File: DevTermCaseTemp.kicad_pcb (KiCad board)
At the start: 2 copper layers, 98.2 x 88.6 mm, 79 parts, among them J1 USB_A, J11 Conn_01x06, J2 EXT_miniPCIe, J3 USB_A, J4 USB_B_Micro, J5 Conn_01x02, J7 DevTermSpeaker, J8 DevTermSpeaker, J9 Conn_02x22_Odd_Even, M2 DevTerm Stock Fan, Q1 BSS138, SW1 SW_DIP_x02, SW2 SW_SPDT, U1 GL850G, U10 4052, U11 4052, U12 TXS0102DCT, U13 USBLC6-2P6, U14 USBLC6-2P6, U15 USBLC6-2P6, U16 USBLC6-2P6, U17 USBLC6-2P6, U18 USBLC6-2P6, U2 SY6280, U3 SY6280, U4 DS1307+, U5 MCP23008-xSO, U6 CH340N, U7 4052, U8 4052, U9 EMC2301-1-ACZL-TR, Y1 12MHz, Y2 32.768KHz

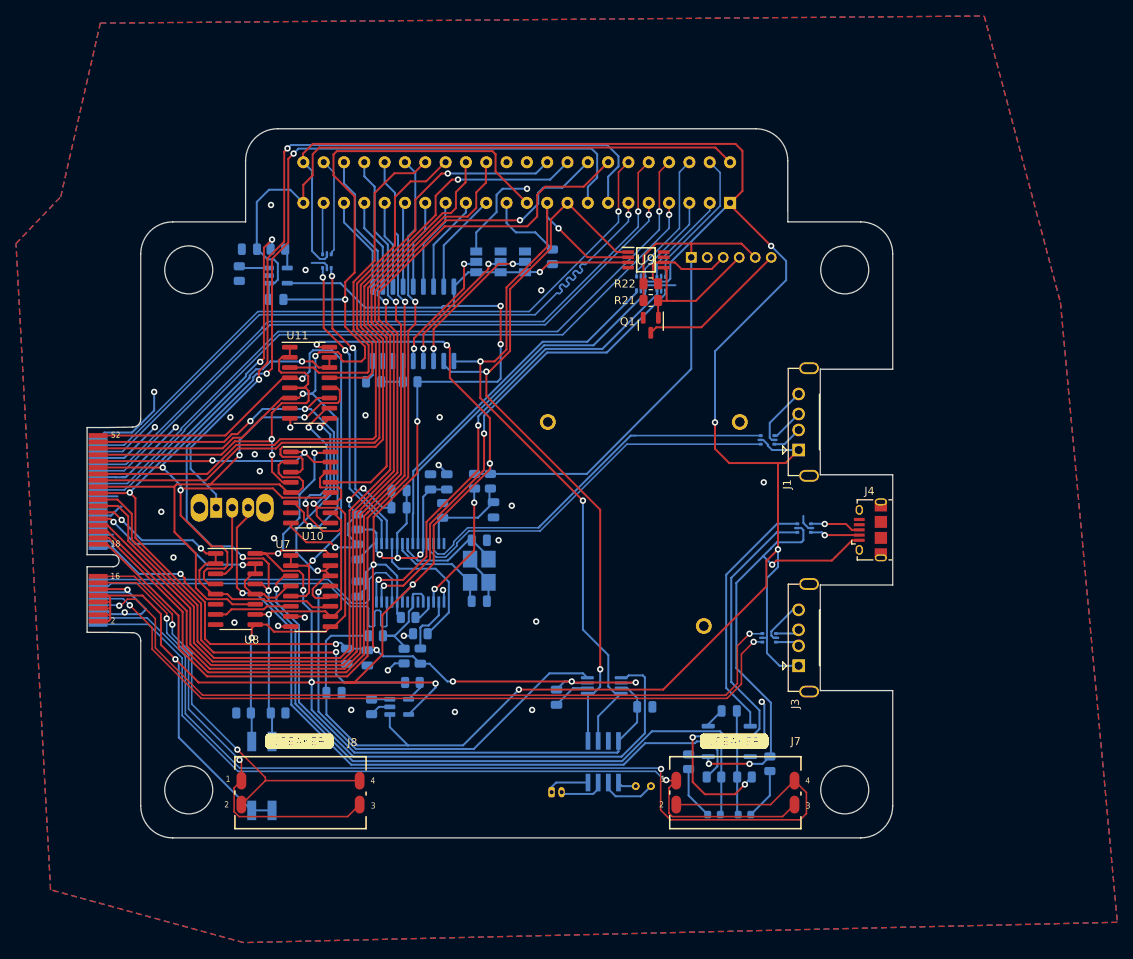
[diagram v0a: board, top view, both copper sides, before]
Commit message: Added bypass caps for USB ESD surge protection as specified in datasheet.
+ Updated silkscreen for version and serial number
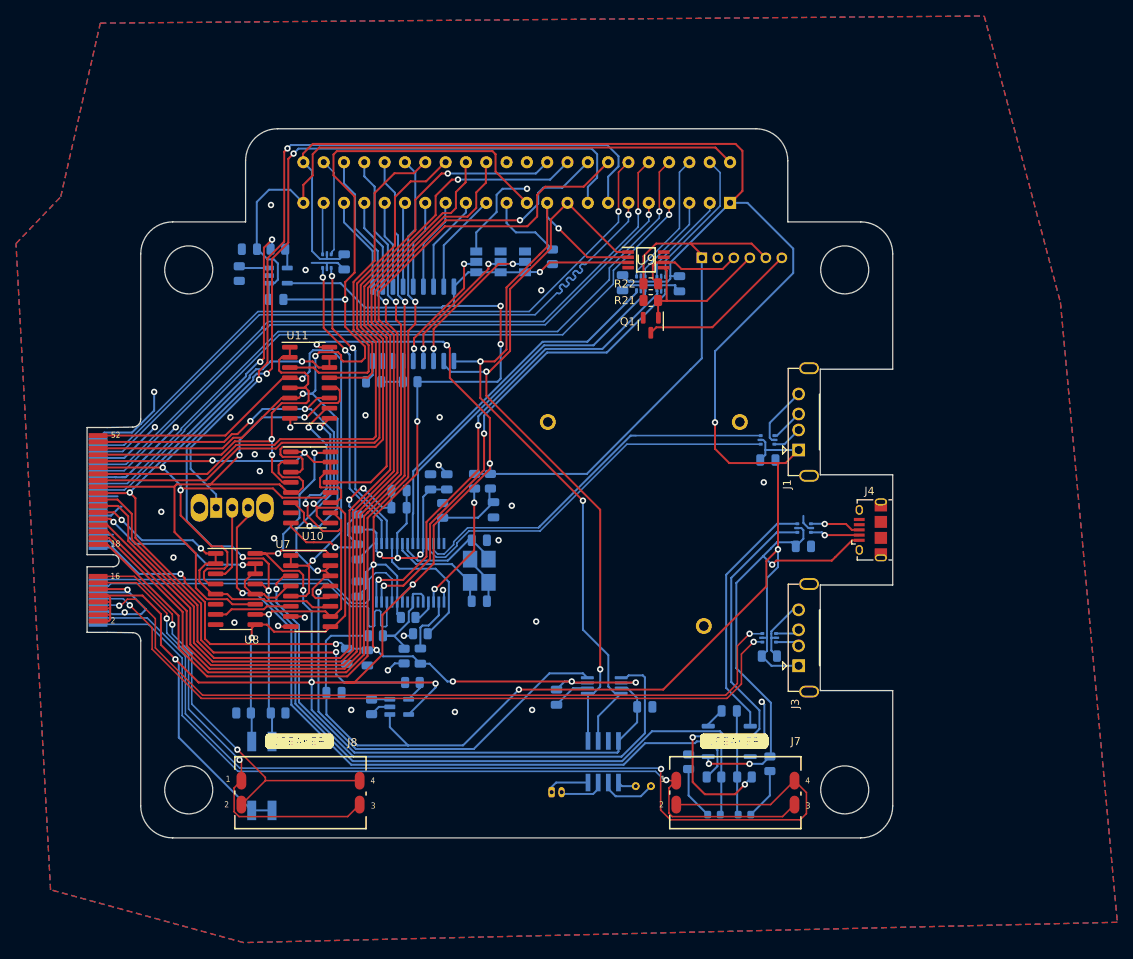
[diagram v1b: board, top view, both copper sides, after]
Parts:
- added C18: 100nF, Capacitor_SMD:C_0805_2012Metric, B.Cu at (175.4, 116.1)
- added C19: 100nF, Capacitor_SMD:C_0805_2012Metric, B.Cu at (175.3, 91.6)
- added C20: 100nF, Capacitor_SMD:C_0805_2012Metric, B.Cu at (164.2, 69.5)
- added C21: 100nF, Capacitor_SMD:C_0805_2012Metric, B.Cu at (157.1, 69.4)
- added C22: 100nF, Capacitor_SMD:C_0805_2012Metric, B.Cu at (122.3, 66.8)
- added C23: 100nF, Capacitor_SMD:C_0805_2012Metric, B.Cu at (179.7, 102.4)
- moved J11 1.32 mm to (167.0, 66.3)
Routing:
- net +5VP: track 271.3 -> 282.4 mm, vias 4 -> 3
- net GND: track 172.4 -> 181.5 mm
- net +5V: track 335.4 -> 337.9 mm
- net Net-(J11-Pin_6): track 19.0 -> 20.3 mm
- net Net-(J11-Pin_4): track 18.9 -> 20.2 mm
- net Net-(J11-Pin_3): track 12.5 -> 13.8 mm
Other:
- board text added: "DevTerm EXT Cart flip/v1.1"
- board text added: "EXTC-2- ."
- board text added: "Serial Number"
- board text removed: "DevTerm EXT Cart flip/v1.0 Serial No:"
- board text removed: "EXTC-1- ."
